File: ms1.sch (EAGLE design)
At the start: 146 parts, among them IC1 MAX3232EUE, IC2 MAX3380EEUP, J1 POWERPOLE_POWER25A, J10 Radio, J11 A3, J12 A4, J13 A5, J14 A6, J15 A7, J16 D1, J17 D2, J18 D3, J19 D4, J2 ON, J20 D5, J21 D6, J22 D7, J3 LED-EN, J4 RS232, J5 RS485, J6 A1, J7 I2C, J8 A2, J9 TTL_SERIAL, Q1 DMG6602SVT, Q2 DMG6602SVT, Q3 DMG6602SVT, Q4 DMG6602SVT, U1 LT1934ES6TRMPBF, U2 LT1934ES6TRMPBF, U3 DS3231SN, U4 ISL3179EIBZ, X1 KUSBVX-BS1N

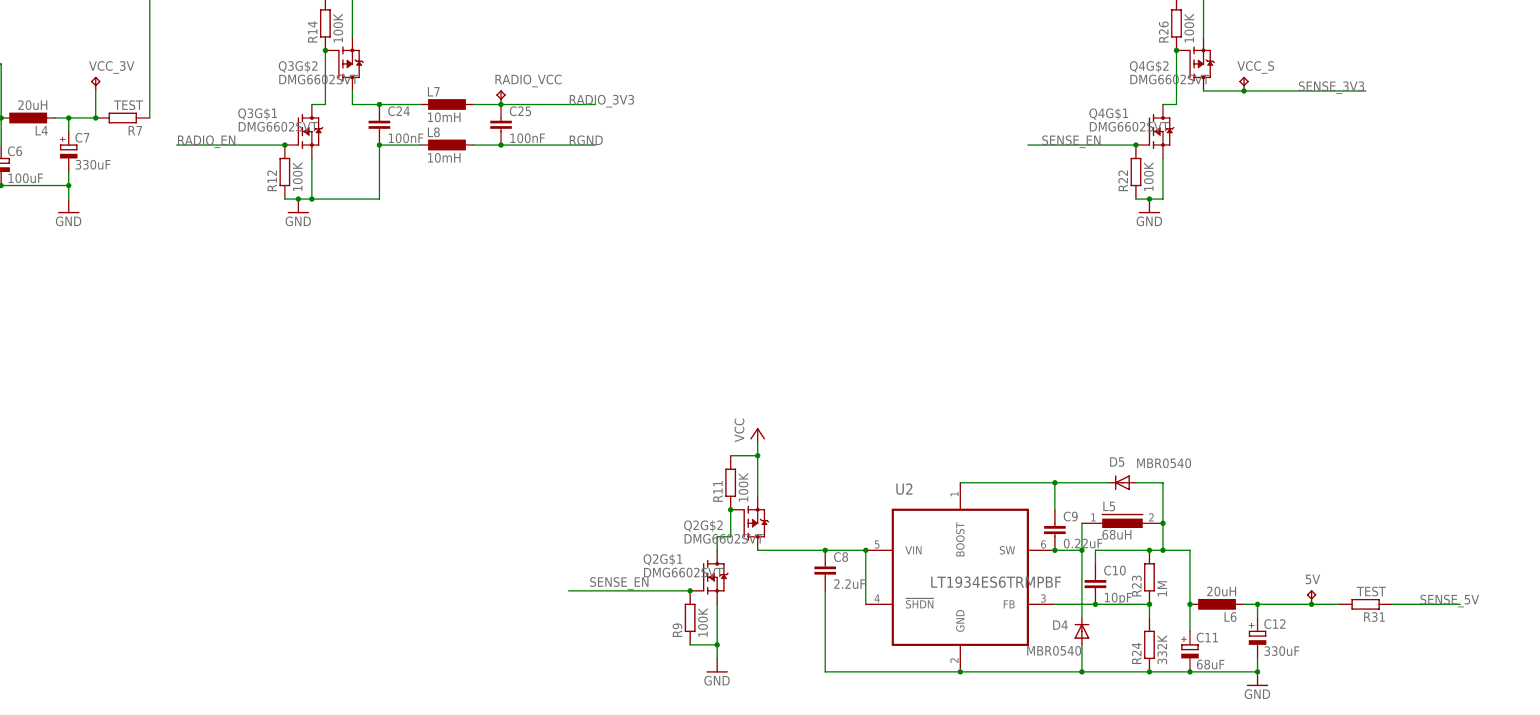
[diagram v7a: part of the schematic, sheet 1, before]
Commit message: more smoothing to 5v rail
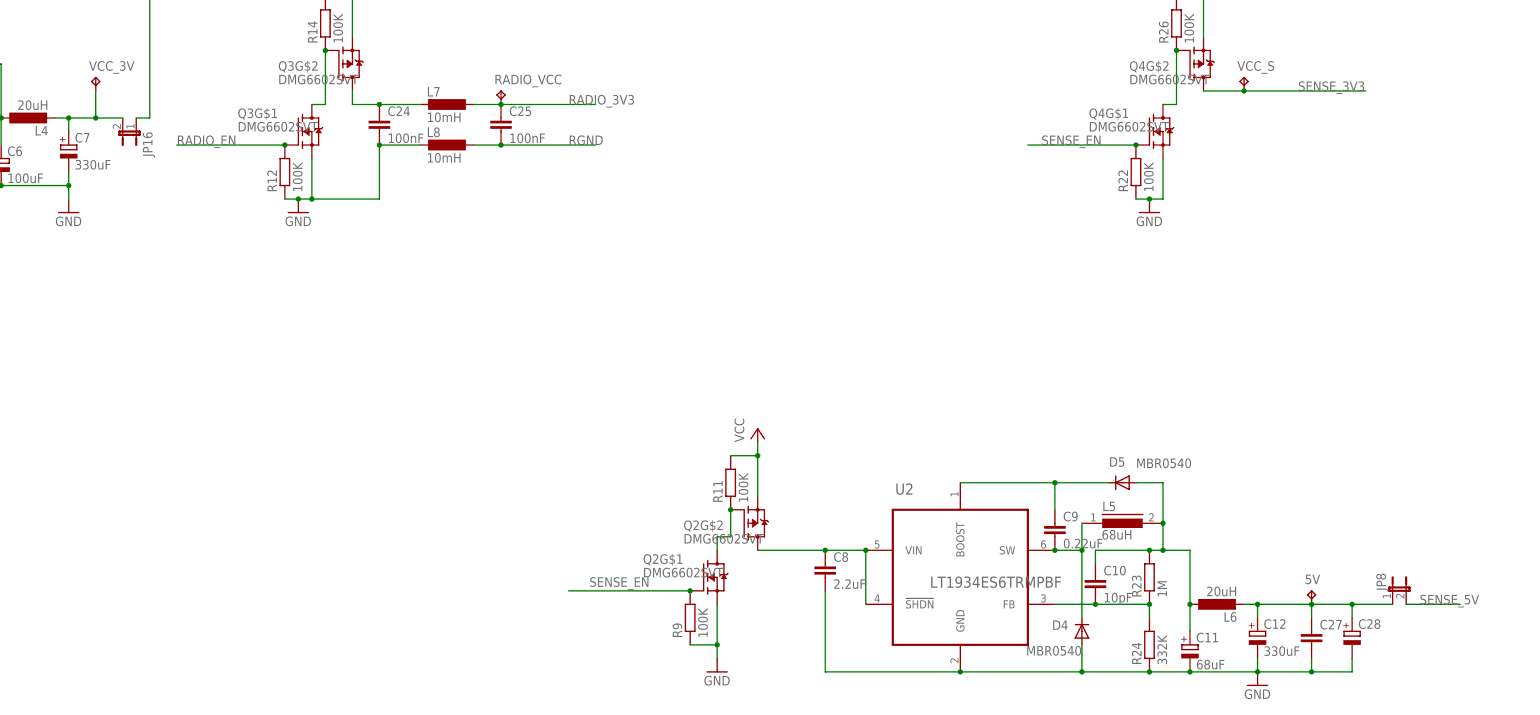
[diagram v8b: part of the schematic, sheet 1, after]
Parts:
- removed R31, R7: TEST, resistor:R-EU_R0805
- added C27: (no value), resistor:C-EUC0805
- added C28: (no value), resistor:CPOL-EUB/3528-21R
- added JP16, JP8: (no value), SparkFun-Passives:JUMPER-2SMD-NO
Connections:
- net GND: now also C27.2, C28.-
- net N$13: now also JP16.2; no longer R7.2
- net N$14: now also C27.1, C28.+, JP8.1; no longer R31.2
- net SENSE_5V: now also JP8.2; no longer R31.1
- net VCC_3V3: now also JP16.1; no longer R7.1
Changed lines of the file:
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@@
 <part name="J9" library="farnell-parts" deviceset="5-PIN-MOLEX" device="" value="TTL_SERIAL"/>
 <part name="GND9" library="supply1" deviceset="GND" device=""/>
-<part name="R7" library="resistor" deviceset="R-EU_" device="R0805" value="TEST"/>
 <part name="R4" library="resistor" deviceset="R-EU_" device="R0805" value="51K"/>
 <part name="R3" library="resistor" deviceset="R-EU_" device="R0805" value="100K"/>
@@
 <part name="R1" library="resistor" deviceset="R-EU_" device="R0805" value="100K"/>
 <part name="R2" library="resistor" deviceset="R-EU_" device="R0805" value="100K"/>
-<part name="R31" library="resistor" deviceset="R-EU_" device="R0805" value="TEST"/>
 <part name="P+2" library="supply1" deviceset="VCC" device=""/>
 <part name="Q1" library="farnell-parts" deviceset="DMG6602SVT" device=""/>
@@
 <part name="C26" library="resistor" deviceset="C-EU" device="C0805" value="100nF"/>
 <part name="R33" library="resistor" deviceset="R-EU_" device="R0805" value="1K"/>
+<part name="C27" library="resistor" deviceset="C-EU" device="C0805"/>
+<part name="C28" library="resistor" deviceset="CPOL-EU" device="B/3528-21R"/>
+<part name="JP8" library="SparkFun-Passives" deviceset="JUMPER-2" device="SMD-NO"/>
+<part name="JP16" library="SparkFun-Passives" deviceset="JUMPER-2" device="SMD-NO"/>
 </parts>
 <sheets>
@@
 <instance part="Q3" gate="G$1" x="154.94" y="149.86"/>
 <instance part="Q3" gate="G$2" x="160.02" y="162.56"/>
-<instance part="R7" gate="G$1" x="119.38" y="152.4" rot="R180"/>
 <instance part="R4" gate="G$1" x="165.1" y="205.74" rot="R90"/>
 <instance part="R3" gate="G$1" x="165.1" y="215.9" rot="R90"/>
@@
 <instance part="R1" gate="G$1" x="139.7" y="208.28" rot="R90"/>
 <instance part="R2" gate="G$1" x="147.32" y="233.68" rot="R90"/>
-<instance part="R31" gate="G$1" x="353.06" y="60.96" rot="R180"/>
 <instance part="P+2" gate="VCC" x="27.94" y="177.8"/>
 <instance part="Q1" gate="G$1" x="144.78" y="215.9"/>
@@
 <instance part="L8" gate="G$1" x="180.34" y="147.32" rot="R270"/>
 <instance part="AGND" gate="G$1" x="83.82" y="205.74"/>
+<instance part="C27" gate="G$1" x="342.9" y="55.88"/>
+<instance part="C28" gate="G$1" x="350.52" y="55.88"/>
+<instance part="JP8" gate="A" x="358.14" y="63.5"/>
+<instance part="JP16" gate="A" x="121.92" y="149.86" rot="R180"/>
 </instances>
 <busses>
@@
 <junction x="332.74" y="48.26"/>
 <junction x="320.04" y="48.26"/>
+<pinref part="C28" gate="G$1" pin="-"/>
+<wire x1="332.74" y1="48.26" x2="342.9" y2="48.26" width="0.1524" layer="91"/>
+<wire x1="342.9" y1="48.26" x2="350.52" y2="48.26" width="0.1524" layer="91"/>
+<wire x1="350.52" y1="48.26" x2="350.52" y2="50.8" width="0.1524" layer="91"/>
+<pinref part="C27" gate="G$1" pin="2"/>
+<wire x1="342.9" y1="50.8" x2="342.9" y2="48.26" width="0.1524" layer="91"/>
+<junction x="342.9" y="48.26"/>
 </segment>
 <segment>
@@
 <net name="VCC_3V3" class="0">
 <segment>
-<pinref part="R7" gate="G$1" pin="1"/>
 <pinref part="Q3" gate="G$2" pin="S"/>
 <wire x1="162.56" y1="167.64" x2="162.56" y2="175.26" width="0.1524" layer="91"/>
@@
 <junction x="162.56" y="175.26"/>
 <junction x="317.5" y="175.26"/>
+<pinref part="JP16" gate="A" pin="1"/>
+<wire x1="121.92" y1="152.4" x2="124.46" y2="152.4" width="0.1524" layer="91"/>
 </segment>
 <segment>
@@
 </segment>
 <segment>
-<pinref part="R31" gate="G$1" pin="1"/>
-<wire x1="358.14" y1="60.96" x2="370.84" y2="60.96" width="0.1524" layer="91"/>
+<wire x1="360.68" y1="60.96" x2="370.84" y2="60.96" width="0.1524" layer="91"/>
 <label x="363.22" y="60.96" size="1.778" layer="95"/>
+<pinref part="JP8" gate="A" pin="2"/>
 </segment>
 </net>
@@
 <wire x1="109.22" y1="149.86" x2="109.22" y2="152.4" width="0.1524" layer="91"/>
 <pinref part="C7" gate="G$1" pin="+"/>
-<pinref part="R7" gate="G$1" pin="2"/>
 <wire x1="114.3" y1="152.4" x2="109.22" y2="152.4" width="0.1524" layer="91"/>
 <pinref part="VCC_3V" gate="G$1" pin="TP"/>
 <wire x1="114.3" y1="152.4" x2="114.3" y2="157.48" width="0.1524" layer="91"/>
+<junction x="109.22" y="152.4"/>
+<pinref part="JP16" gate="A" pin="2"/>
+<wire x1="119.38" y1="152.4" x2="114.3" y2="152.4" width="0.1524" layer="91"/>
 <junction x="114.3" y="152.4"/>
-<junction x="109.22" y="152.4"/>
 </segment>
 </net>
@@
 <pinref part="5V" gate="G$1" pin="TP"/>
 <wire x1="332.74" y1="60.96" x2="342.9" y2="60.96" width="0.1524" layer="91"/>
-<pinref part="R31" gate="G$1" pin="2"/>
-<wire x1="342.9" y1="60.96" x2="347.98" y2="60.96" width="0.1524" layer="91"/>
+<wire x1="342.9" y1="60.96" x2="350.52" y2="60.96" width="0.1524" layer="91"/>
 <junction x="332.74" y="60.96"/>
 <junction x="342.9" y="60.96"/>
-</segment>
-</net>
+<pinref part="C27" gate="G$1" pin="1"/>
+<wire x1="342.9" y1="60.96" x2="342.9" y2="58.42" width="0.1524" layer="91"/>
+<pinref part="C28" gate="G$1" pin="+"/>
+<wire x1="350.52" y1="58.42" x2="350.52" y2="60.96" width="0.1524" layer="91"/>
+<junction x="350.52" y="60.96"/>
+<pinref part="JP8" gate="A" pin="1"/>
+<wire x1="358.14" y1="60.96" x2="350.52" y2="60.96" width="0.1524" layer="91"/>
+</segment>
+</net>
